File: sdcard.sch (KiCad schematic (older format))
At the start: 8 parts, among them J11 DM3D-SF

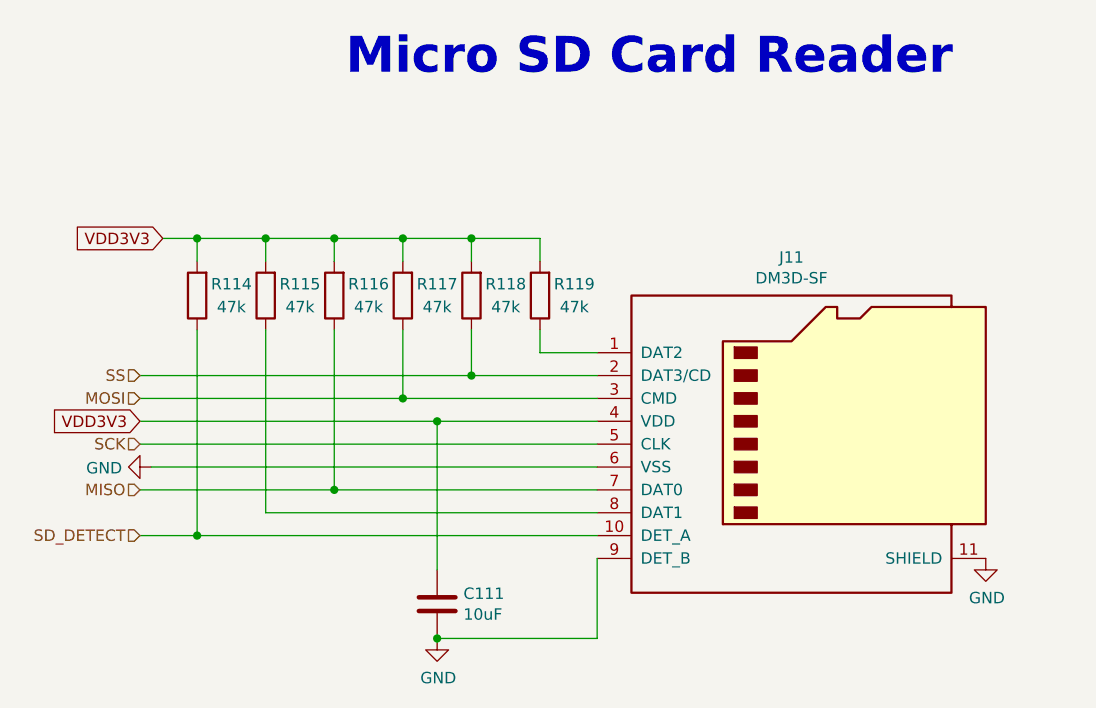
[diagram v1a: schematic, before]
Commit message: Add PD resistor to BOOT PIN
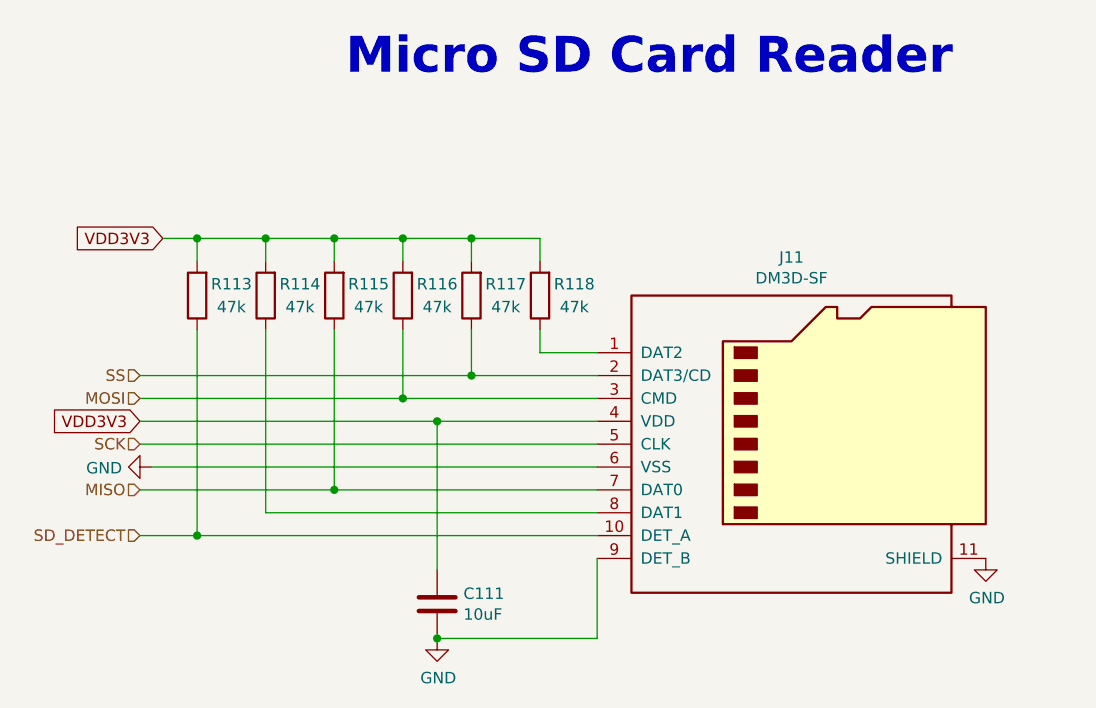
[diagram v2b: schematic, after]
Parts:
- renumbered R114 to R113, R115 to R114, R116 to R115, R117 to R116, R118 to R117, R119 to R118
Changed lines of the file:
@@
 EESchema Schematic File Version 4
 LIBS:heteromycin-cache
-EELAYER 29 0
+EELAYER 26 0
 EELAYER END
 $Descr A4 11693 8268
@@
 AR Path="/5BC77F8A/5BC83407" Ref="R?"  Part="1"
 AR Path="/5BC77F8D/5BC83407" Ref="R?"  Part="1"
-AR Path="/5BC78E83/5BC83407" Ref="R119"  Part="1"
-F 0 "R119" H 4700 2450 50  0000 C CNN
+AR Path="/5BC78E83/5BC83407" Ref="R118"  Part="1"
+F 0 "R118" H 4700 2450 50  0000 C CNN
 F 1 "47k" H 4700 2550 50  0000 C CNN
 F 2 "Resistor_SMD:R_0603_1608Metric" V 4780 2500 50  0001 C CNN
@@
 AR Path="/5BC77F8A/5BC8393A" Ref="R?"  Part="1"
 AR Path="/5BC77F8D/5BC8393A" Ref="R?"  Part="1"
-AR Path="/5BC78E83/5BC8393A" Ref="R118"  Part="1"
-F 0 "R118" H 4400 2450 50  0000 C CNN
+AR Path="/5BC78E83/5BC8393A" Ref="R117"  Part="1"
+F 0 "R117" H 4400 2450 50  0000 C CNN
 F 1 "47k" H 4400 2550 50  0000 C CNN
 F 2 "Resistor_SMD:R_0603_1608Metric" V 4480 2500 50  0001 C CNN
@@
 AR Path="/5BC77F8A/5BC842EF" Ref="R?"  Part="1"
 AR Path="/5BC77F8D/5BC842EF" Ref="R?"  Part="1"
-AR Path="/5BC78E83/5BC842EF" Ref="R117"  Part="1"
-F 0 "R117" H 4100 2450 50  0000 C CNN
+AR Path="/5BC78E83/5BC842EF" Ref="R116"  Part="1"
+F 0 "R116" H 4100 2450 50  0000 C CNN
 F 1 "47k" H 4100 2550 50  0000 C CNN
 F 2 "Resistor_SMD:R_0603_1608Metric" V 4180 2500 50  0001 C CNN
@@
 AR Path="/5BC77F8A/5BC84424" Ref="R?"  Part="1"
 AR Path="/5BC77F8D/5BC84424" Ref="R?"  Part="1"
-AR Path="/5BC78E83/5BC84424" Ref="R116"  Part="1"
-F 0 "R116" H 3800 2450 50  0000 C CNN
+AR Path="/5BC78E83/5BC84424" Ref="R115"  Part="1"
+F 0 "R115" H 3800 2450 50  0000 C CNN
 F 1 "47k" H 3800 2550 50  0000 C CNN
 F 2 "Resistor_SMD:R_0603_1608Metric" V 3880 2500 50  0001 C CNN
@@
 AR Path="/5BC77F8A/5BC8859F" Ref="R?"  Part="1"
 AR Path="/5BC77F8D/5BC8859F" Ref="R?"  Part="1"
-AR Path="/5BC78E83/5BC8859F" Ref="R115"  Part="1"
-F 0 "R115" H 3500 2450 50  0000 C CNN
+AR Path="/5BC78E83/5BC8859F" Ref="R114"  Part="1"
+F 0 "R114" H 3500 2450 50  0000 C CNN
 F 1 "47k" H 3500 2550 50  0000 C CNN
 F 2 "Resistor_SMD:R_0603_1608Metric" V 3580 2500 50  0001 C CNN
@@
 AR Path="/5BC77F8A/5C0666FE" Ref="R?"  Part="1"
 AR Path="/5BC77F8D/5C0666FE" Ref="R?"  Part="1"
-AR Path="/5BC78E83/5C0666FE" Ref="R114"  Part="1"
-F 0 "R114" H 3200 2450 50  0000 C CNN
+AR Path="/5BC78E83/5C0666FE" Ref="R113"  Part="1"
+F 0 "R113" H 3200 2450 50  0000 C CNN
 F 1 "47k" H 3200 2550 50  0000 C CNN
 F 2 "Resistor_SMD:R_0603_1608Metric" V 3280 2500 50  0001 C CNN
